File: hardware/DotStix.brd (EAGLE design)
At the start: 20.3 x 50 mm, 15 parts, among them U1 ATMEGA328P-MU-QFN32

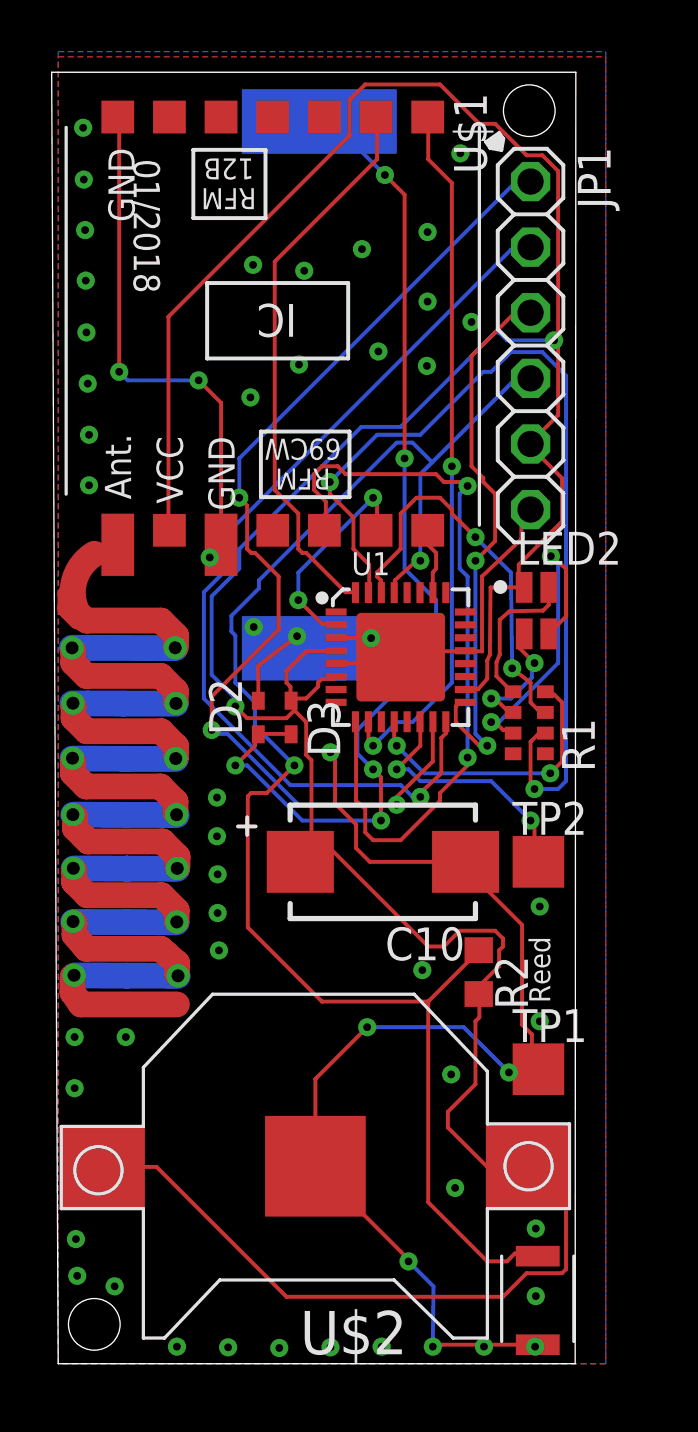
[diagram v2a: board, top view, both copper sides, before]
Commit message: Add HexID, second reed on rear side
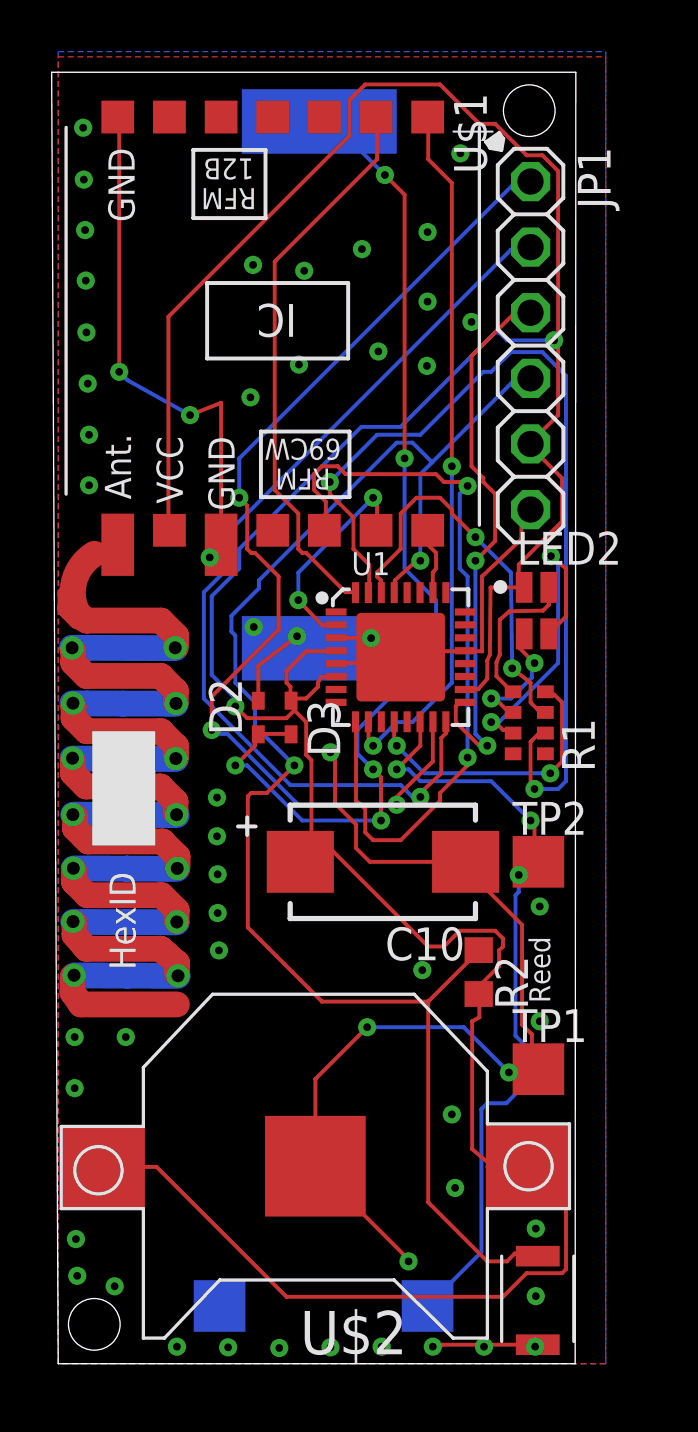
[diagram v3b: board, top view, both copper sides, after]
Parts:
- added TP3, TP4: TPTP20SQ, testpad:TP20SQ
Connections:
- net GND: now also TP3.TP
- net REED: now also TP4.TP
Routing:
- net REED: track 10.3 -> 32.0 mm, vias 2 -> 3
- net GND: track 89.3 -> 85.7 mm
- net +3V3: track 139.1 -> 138.5 mm
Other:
- board text added: "HexID"
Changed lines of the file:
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@@
 <rectangle x1="7.4803" y1="9.8679" x2="8.6487" y2="9.8933" layer="22" rot="R180"/>
 <text x="5.2324" y="44.0436" size="1.27" layer="22" rot="MR270" align="center">Mihai Galos</text>
-<text x="3.429" y="44.0436" size="1.016" layer="21" rot="SR270" align="center">01/2018</text>
 <text x="9.6774" y="11.4046" size="1.016" layer="22" rot="MR0" align="center">DotStix v0.2.1</text>
 <circle x="17.1196" y="30.0736" radius="0.193440625" width="0.1524" layer="21"/>
@@
 <dimension x1="19.99" y1="50.0026" x2="20.0916" y2="0" x3="35.939746875" y3="25.033603125" textsize="1.778" layer="47"/>
 <dimension x1="0" y1="0" x2="20.0154" y2="0" x3="10.0077" y3="-3.2766" textsize="1.778" layer="47"/>
+<text x="3.0226" y="44.0436" size="1.016" layer="22" rot="MR270" align="center">01/2018</text>
+<text x="2.4892" y="17.145" size="1.016" layer="21" rot="SR90" align="center">HexID</text>
+<rectangle x1="1.3208" y1="20.066" x2="3.7592" y2="24.4856" layer="21"/>
 </plain>
 <attributes>
@@
 <element name="C10" library="adafruit" package="CT7343" value="1500uF 4V" x="12.573" y="19.431" rot="R180"/>
 <element name="D3" library="diode" package="SOD523" value="" x="9.017" y="25.0698" rot="R270"/>
+<element name="TP3" library="testpad" package="TP20SQ" value="TPTP20SQ" x="6.2484" y="2.2352" rot="MR270">
+<attribute name="TP_SIGNAL_NAME" value="" x="6.2484" y="2.2352" size="1.016" layer="28" rot="MR270" display="off"/>
+</element>
+<element name="TP4" library="testpad" package="TP20SQ" value="TPTP20SQ" x="14.3002" y="2.2352" rot="MR270">
+<attribute name="TP_SIGNAL_NAME" value="" x="14.3002" y="2.2352" size="1.016" layer="28" rot="MR270" display="off"/>
+</element>
 </elements>
 <signals>
@@
 <wire x1="10.1092" y1="28.0924" x2="10.1092" y2="27.6968" width="0.1524" layer="16"/>
 <wire x1="6.3058" y1="31.7074" x2="6.3058" y2="37.2044" width="0.1524" layer="1"/>
-<wire x1="6.3058" y1="37.2044" x2="5.4356" y2="38.0746" width="0.1524" layer="1"/>
-<via x="5.4356" y="38.0746" extent="1-16" drill="0.3"/>
-<wire x1="5.4356" y1="38.0746" x2="2.6924" y2="38.0746" width="0.1524" layer="16"/>
+<wire x1="6.3058" y1="37.2044" x2="5.1054" y2="36.7284" width="0.1524" layer="1"/>
+<via x="5.1054" y="36.7284" extent="1-16" drill="0.3"/>
+<wire x1="5.1054" y1="36.7284" x2="2.6924" y2="38.0746" width="0.1524" layer="16"/>
 <wire x1="2.6924" y1="38.0746" x2="2.3622" y2="38.4048" width="0.1524" layer="16"/>
 <via x="2.3622" y="38.4048" extent="1-16" drill="0.3"/>
@@
 <wire x1="14.859" y1="0.7366" x2="14.5034" y2="0.6604" width="0.1524" layer="1"/>
 <via x="14.5034" y="0.6604" extent="1-16" drill="0.3"/>
-<wire x1="14.5034" y1="0.6604" x2="14.5288" y2="2.9972" width="0.1524" layer="16"/>
-<wire x1="14.5288" y1="2.9972" x2="13.5636" y2="3.9624" width="0.1524" layer="16"/>
 <via x="13.5636" y="3.9624" extent="1-16" drill="0.3"/>
 <wire x1="13.5636" y1="3.9624" x2="13.5636" y2="4.0386" width="0.1524" layer="1"/>
@@
 <via x="18.6436" y="17.7038" extent="1-16" drill="0.3"/>
 <via x="15.367" y="6.8072" extent="1-16" drill="0.3"/>
-<via x="15.2146" y="11.2014" extent="1-16" drill="0.3"/>
+<via x="15.24" y="9.652" extent="1-16" drill="0.3"/>
 <via x="14.097" y="15.24" extent="1-16" drill="0.3"/>
 <via x="6.1468" y="21.9202" extent="1-16" drill="0.3"/>
@@
 <via x="9.3218" y="38.6842" extent="1-16" drill="0.3"/>
 <via x="9.525" y="42.3164" extent="1-16" drill="0.3"/>
+<contactref element="TP3" pad="TP"/>
 </signal>
 <signal name="SDA">
@@
 <contactref element="U$1" pad="SCK"/>
 <contactref element="U1" pad="2"/>
-<wire x1="10.2108" y1="28.6512" x2="10.668" y2="28.6512" width="0.1524" layer="1"/>
-<wire x1="9.2964" y1="29.5656" x2="10.2108" y2="28.6512" width="0.1524" layer="1"/>
+<wire x1="10.2108" y1="28.6004" x2="10.668" y2="28.6004" width="0.1524" layer="1"/>
+<wire x1="9.2964" y1="29.5656" x2="10.2108" y2="28.6004" width="0.1524" layer="1"/>
 <wire x1="9.2964" y1="30.6324" x2="9.2964" y2="29.5656" width="0.1524" layer="16"/>
 <wire x1="12.192" y1="33.528" x2="9.2964" y2="30.6324" width="0.1524" layer="16"/>
 <wire x1="12.3444" y1="33.3756" x2="12.192" y2="33.528" width="0.1524" layer="1"/>
 <wire x1="12.3444" y1="32.3088" x2="12.3444" y2="33.3756" width="0.1524" layer="1"/>
-<wire x1="10.668" y1="28.6512" x2="10.7588" y2="28.6058" width="0.1524" layer="1"/>
+<wire x1="10.668" y1="28.6004" x2="10.7588" y2="28.6058" width="0.1524" layer="1"/>
 <wire x1="12.3444" y1="32.3088" x2="12.3058" y2="32.267" width="0.1524" layer="1"/>
 <via x="9.2964" y="29.5656" extent="1-16" drill="0.3"/>
@@
 <wire x1="10.0584" y1="26.2128" x2="9.6012" y2="25.7556" width="0.1524" layer="1"/>
 <wire x1="10.0584" y1="26.3652" x2="10.0584" y2="26.2128" width="0.1524" layer="1"/>
-<wire x1="10.2108" y1="26.5176" x2="10.0584" y2="26.3652" width="0.1524" layer="1"/>
-<wire x1="10.668" y1="26.5176" x2="10.2108" y2="26.5176" width="0.1524" layer="1"/>
+<wire x1="10.1854" y1="26.5938" x2="10.0584" y2="26.3652" width="0.1524" layer="1"/>
+<wire x1="10.6426" y1="26.5938" x2="10.1854" y2="26.5938" width="0.1524" layer="1"/>
 <wire x1="9.144" y1="25.7556" x2="9.017" y2="25.6698" width="0.1524" layer="1"/>
-<wire x1="10.668" y1="26.5176" x2="10.7588" y2="26.6058" width="0.1524" layer="1"/>
+<wire x1="10.6426" y1="26.5938" x2="10.7588" y2="26.6058" width="0.1524" layer="1"/>
 <wire x1="9.6012" y1="27.5844" x2="10.668" y2="27.5844" width="0.1524" layer="1"/>
 <wire x1="8.8392" y1="26.8224" x2="9.6012" y2="27.5844" width="0.1524" layer="1"/>
@@
 <wire x1="9.4488" y1="19.5072" x2="9.373" y2="19.431" width="0.1524" layer="1"/>
 <wire x1="16.3068" y1="13.4112" x2="16.3068" y2="14.1732" width="0.1524" layer="1"/>
-<wire x1="16.1544" y1="13.2588" x2="16.3068" y2="13.4112" width="0.1524" layer="1"/>
-<wire x1="16.1544" y1="10.8204" x2="16.1544" y2="13.2588" width="0.1524" layer="1"/>
-<wire x1="15.0876" y1="9.7536" x2="16.1544" y2="10.8204" width="0.1524" layer="1"/>
-<wire x1="15.0876" y1="9.144" x2="15.0876" y2="9.7536" width="0.1524" layer="1"/>
-<wire x1="16.6116" y1="7.62" x2="15.0876" y2="9.144" width="0.1524" layer="1"/>
-<wire x1="18.1356" y1="7.62" x2="16.6116" y2="7.62" width="0.1524" layer="1"/>
+<wire x1="16.0274" y1="13.2588" x2="16.3068" y2="13.4112" width="0.1524" layer="1"/>
+<wire x1="18.1356" y1="7.62" x2="16.8402" y2="7.62" width="0.1524" layer="1"/>
+<wire x1="16.8402" y1="7.62" x2="16.6116" y2="7.62" width="0.1524" layer="1"/>
 <wire x1="16.3068" y1="14.1732" x2="16.2814" y2="14.3138" width="0.1524" layer="1"/>
 <wire x1="18.1356" y1="7.62" x2="18.1568" y2="7.6454" width="0.1524" layer="1"/>
@@
 <wire x1="16.7132" y1="27.4574" x2="16.7386" y2="30.0541" width="0.1524" layer="1"/>
 <wire x1="16.7386" y1="30.0541" x2="18.0391" y2="30.0592" width="0.1524" layer="1"/>
+<wire x1="16.0274" y1="13.2588" x2="16.0274" y2="8.3058" width="0.1524" layer="1"/>
+<wire x1="16.0274" y1="8.3058" x2="16.8402" y2="7.62" width="0.1524" layer="1"/>
 </signal>
 <signal name="ADCENA">
@@
 </signal>
 <signal name="REED">
-<contactref element="TP2" pad="TP"/>
 <contactref element="U1" pad="14"/>
 <wire x1="14.0208" y1="23.9268" x2="14.0208" y2="24.8412" width="0.1524" layer="1"/>
@@
 <wire x1="18.8976" y1="19.5072" x2="18.4404" y2="19.9644" width="0.1524" layer="1"/>
 <wire x1="14.0208" y1="24.8412" x2="14.0088" y2="24.8558" width="0.1524" layer="1"/>
-<wire x1="18.8976" y1="19.5072" x2="18.5928" y2="19.431" width="0.1524" layer="1"/>
 <via x="13.1064" y="23.0124" extent="1-16" drill="0.3"/>
 <via x="18.288" y="21.0312" extent="1-16" drill="0.3"/>
+<contactref element="TP4" pad="TP"/>
+<contactref element="TP2" pad="TP"/>
+<wire x1="18.5928" y1="19.431" x2="17.8308" y2="19.431" width="0.1524" layer="1"/>
+<wire x1="17.8308" y1="19.431" x2="17.7038" y2="19.304" width="0.1524" layer="1"/>
+<wire x1="18.4404" y1="19.9644" x2="18.3642" y2="19.9644" width="0.1524" layer="1"/>
+<wire x1="18.3642" y1="19.9644" x2="17.8308" y2="19.431" width="0.1524" layer="1"/>
+<wire x1="18.5928" y1="19.431" x2="18.1864" y2="19.431" width="0.1524" layer="1"/>
+<wire x1="18.1864" y1="19.431" x2="17.7292" y2="18.9738" width="0.1524" layer="1"/>
+<wire x1="17.7292" y1="18.9738" x2="17.78" y2="18.9738" width="0.1524" layer="1"/>
+<wire x1="17.78" y1="18.9738" x2="17.8308" y2="18.923" width="0.1524" layer="1"/>
+<via x="17.8308" y="18.923" extent="1-16" drill="0.3"/>
+<wire x1="17.8308" y1="18.923" x2="17.8308" y2="18.2626" width="0.1524" layer="16"/>
+<wire x1="17.8308" y1="18.2626" x2="17.7038" y2="18.1356" width="0.1524" layer="16"/>
+<wire x1="17.7038" y1="18.1356" x2="17.7038" y2="12.7" width="0.1524" layer="16"/>
+<wire x1="17.7038" y1="12.7" x2="18.2118" y2="12.192" width="0.1524" layer="16"/>
+<wire x1="18.2118" y1="12.192" x2="18.2118" y2="10.9474" width="0.1524" layer="16"/>
+<wire x1="18.2118" y1="10.9474" x2="17.3482" y2="10.0838" width="0.1524" layer="16"/>
+<wire x1="17.3482" y1="10.0838" x2="16.6116" y2="10.0838" width="0.1524" layer="16"/>
+<wire x1="16.6116" y1="10.0838" x2="16.383" y2="9.8552" width="0.1524" layer="16"/>
+<wire x1="16.383" y1="9.8552" x2="16.383" y2="4.318" width="0.1524" layer="16"/>
+<wire x1="16.383" y1="4.318" x2="14.3002" y2="2.2352" width="0.1524" layer="16"/>
 </signal>
 <signal name="SOLAR_RAW">

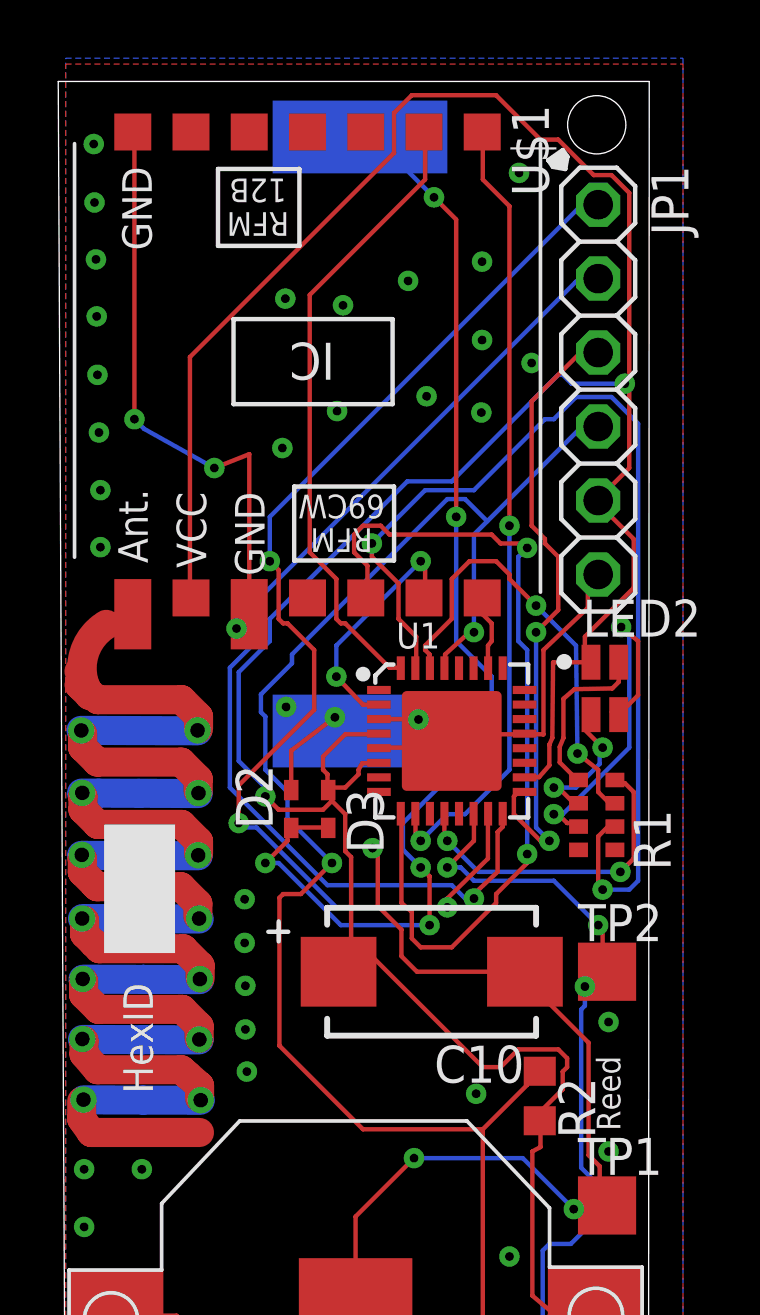
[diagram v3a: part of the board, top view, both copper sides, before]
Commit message: Add photoresistor
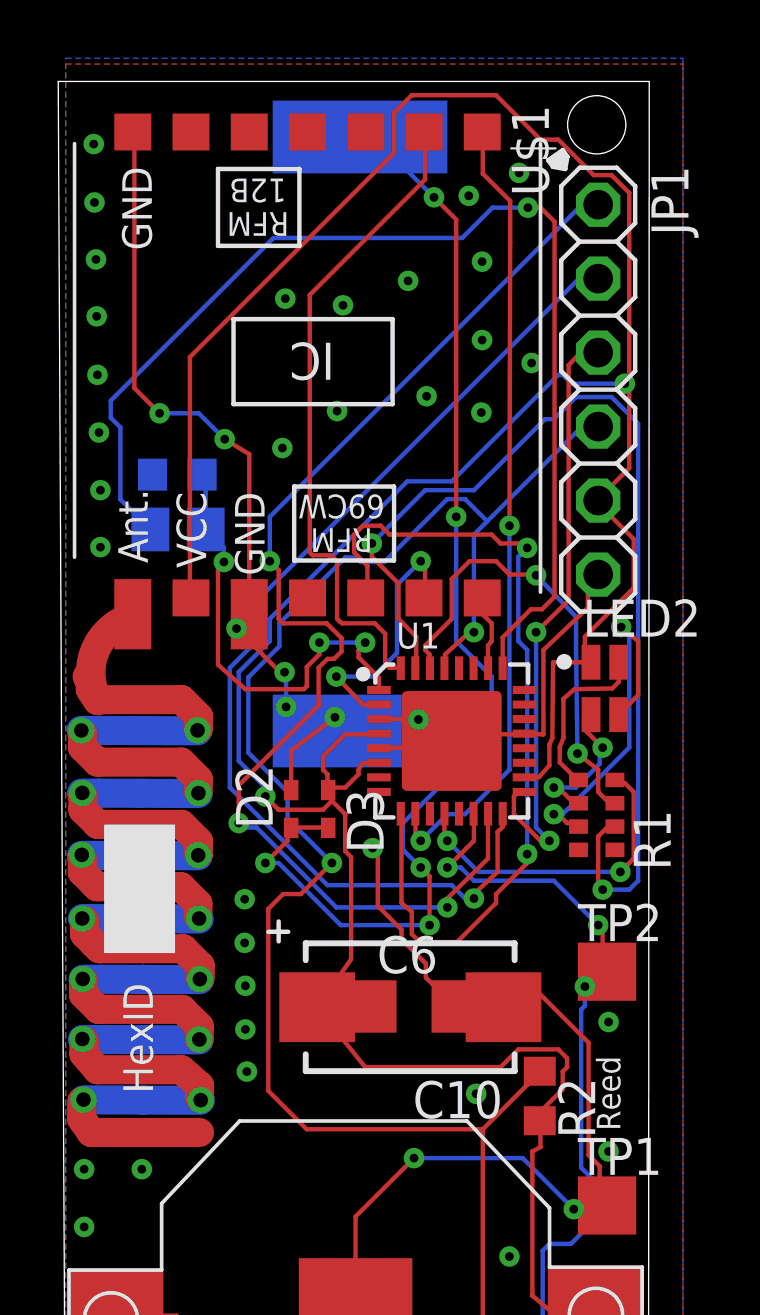
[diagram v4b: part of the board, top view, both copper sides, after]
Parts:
- added C6: 100uF 4V, adafruit:C3216
- added R3: (no value), resistor:R0805
- added R4: 10kΩ, resistor:R0603
- moved C10 1.42 mm to (11.8, 18.2)
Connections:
- removed net MOVE_INT: U1.25
- removed net PUSH: U1.1
- net +3V3: now also C6.1
- net GND: now also C6.2, R4.1
- net LIGHT_SENSE: now also R3.1, R4.2, U1.1; no longer U1.22
- net LIGHT_SENSE_ENA: now also R3.2, U1.25; no longer U1.11
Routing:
- net LIGHT_SENSE_ENA: track 0.00 -> 39.5 mm, vias 0 -> 1
- net LIGHT_SENSE: track 0.00 -> 15.7 mm, vias 0 -> 3
- net GND: track 85.7 -> 89.3 mm, vias 55 -> 57
- net +3V3: track 138.5 -> 142.1 mm
- net RST: track 60.3 -> 63.1 mm
- net MOSI: track 40.2 -> 41.9 mm
- net RIRQ: track 21.7 -> 22.7 mm
- net SCK: track 21.6 -> 20.8 mm
- net RSCK: track 8.38 -> 9.12 mm
- net ANT: track 79.8 -> 79.2 mm

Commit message: Minor info improvements
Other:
- board text added: "If you plan on potting the board in transparent epoxy, the battery's max cycle count ist 1000. Use a 330mF Supercap instead of battery: DSK-3R3H334T-HL"
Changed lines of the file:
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@@
 <setting verticaltext="up"/>
 </settings>
-<grid distance="1" unitdist="mil" unit="mm" style="lines" multiple="1" display="yes" altdistance="0.025" altunitdist="inch" altunit="inch"/>
+<grid distance="0.00254" unitdist="mm" unit="mm" style="lines" multiple="1" display="yes" altdistance="0.025" altunitdist="inch" altunit="inch"/>
 <layers>
 <layer number="1" name="Top" color="4" fill="1" visible="yes" active="yes"/>
@@
 <layer number="45" name="Holes" color="7" fill="1" visible="no" active="yes"/>
 <layer number="46" name="Milling" color="3" fill="1" visible="no" active="yes"/>
-<layer number="47" name="Measures" color="7" fill="1" visible="no" active="yes"/>
+<layer number="47" name="Measures" color="7" fill="1" visible="yes" active="yes"/>
 <layer number="48" name="Document" color="7" fill="1" visible="yes" active="yes"/>
 <layer number="49" name="Reference" color="7" fill="1" visible="no" active="yes"/>
@@
 <text x="2.4892" y="17.145" size="1.016" layer="21" rot="SR90" align="center">HexID</text>
 <rectangle x1="1.3208" y1="20.066" x2="3.7592" y2="24.4856" layer="21"/>
+<text x="-0.06858125" y="59.93891875" size="1.778" layer="48">If you plan on potting the board in transparent epoxy, the battery's max cycle count ist 1000.
+Use a 330mF Supercap instead of battery: DSK-3R3H334T-HL  </text>
 </plain>
 <attributes>
@@
 <wire x1="12.1158" y1="28.0924" x2="10.1092" y2="28.0924" width="0.1524" layer="16"/>
 <wire x1="10.1092" y1="28.0924" x2="10.1092" y2="27.6968" width="0.1524" layer="16"/>
-<wire x1="6.3058" y1="31.7074" x2="6.3058" y2="37.2044" width="0.1524" layer="1"/>
-<wire x1="6.3058" y1="37.2044" x2="5.461" y2="37.719" width="0.1524" layer="1"/>
-<via x="5.461" y="37.719" extent="1-16" drill="0.3"/>
+<wire x1="6.3058" y1="31.7074" x2="6.3312" y2="36.798" width="0.1524" layer="1"/>
+<wire x1="6.3312" y1="36.798" x2="6.0452" y2="37.0586" width="0.1524" layer="1"/>
+<via x="6.0452" y="37.0586" extent="1-16" drill="0.3"/>
 <wire x1="2.3622" y1="48.2106" x2="2.3058" y2="48.267" width="0.1524" layer="1"/>
 <via x="17.4498" y="11.2776" extent="1-16" drill="0.3"/>
@@
 <via x="3.2258" y="38.608" extent="1-16" drill="0.3"/>
 <wire x1="3.2258" y1="38.608" x2="4.572" y2="38.608" width="0.1524" layer="16"/>
-<wire x1="4.572" y1="38.608" x2="5.461" y2="37.719" width="0.1524" layer="16"/>
+<wire x1="4.572" y1="38.608" x2="6.0452" y2="37.0586" width="0.1524" layer="16"/>
 <wire x1="7.5692" y1="28.5242" x2="7.5692" y2="29.6672" width="0.1524" layer="16"/>
 <wire x1="7.5692" y1="29.6672" x2="7.5184" y2="29.718" width="0.1524" layer="16"/>
